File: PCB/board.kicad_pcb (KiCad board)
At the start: 2 copper layers, 81.6 x 88.8 mm, 165 parts, among them J1 Micro_SD_Card, J10 Conn_01x10, J11 Conn_01x02, J12 Conn_02x04_Odd_Even, J13 Conn_01x02, J14 Conn_01x02, J15 Conn_01x03, J16 Conn_01x02, J17 Conn_01x05, J18 Conn_01x04, J19 Conn_01x04, J2 Conn_ARM_JTAG_SWD_10, J20 Conn_01x02, J21 Conn_01x03, J22 Conn_02x04_Odd_Even, J23 Conn_01x04, J24 Conn_01x04, J25 Conn_01x02, J26 Conn_01x03, J27 Conn_02x04_Odd_Even, J28 Conn_01x04, J29 Conn_01x04, J3 USB_C_Receptacle_USB2.0_14P, J30 Conn_01x02, J31 Conn_01x03, J32 Conn_01x02, J33 Conn_01x02, J34 Conn_01x02, J35 Conn_01x02, J36 Conn_01x02, J37 Conn_01x02, J4 Conn_01x04, J5 Conn_01x04, J6 Conn_01x02, J7 Conn_01x03, J8 Conn_02x04_Odd_Even, J9 Conn_01x10, Q1 IRLML6402, Q2 NMOS, Q3 NMOS, Q4 NMOS, Q5 Q_NMOS_GDS, Q7 Q_NMOS_GDS, SW1 SW_Push, SW2 SW_Push, U1 STM32H743VITx, U2 AP7361C, U4 TMC Stepstick, U5 TMC Stepstick, U6 TMC Stepstick, U7 TMC Stepstick, U8 AP63203WU, Y2 25 MHz

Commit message: some journal stuff and starting the routing
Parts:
- moved H1 0.40 mm to (220.9, 28.1)
- moved H3 0.40 mm to (158.4, 28.1)
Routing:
- added copper zone on In2.Cu, net +3.3V
- added copper zone on In1.Cu, net GND
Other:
- copper layers 2 -> 4
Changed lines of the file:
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@@
 	(layers
 		(0 "F.Cu" signal)
+		(4 "In1.Cu" signal "GND")
+		(6 "In2.Cu" signal "POWER")
 		(2 "B.Cu" signal)
 		(9 "F.Adhes" user "F.Adhesive")
@@
 			)
 			(layer "dielectric 1"
+				(type "prepreg")
+				(thickness 0.1)
+				(material "FR4")
+				(epsilon_r 4.5)
+				(loss_tangent 0.02)
+			)
+			(layer "In1.Cu"
+				(type "copper")
+				(thickness 0.035)
+			)
+			(layer "dielectric 2"
 				(type "core")
-				(thickness 1.51)
+				(thickness 1.24)
+				(material "FR4")
+				(epsilon_r 4.5)
+				(loss_tangent 0.02)
+			)
+			(layer "In2.Cu"
+				(type "copper")
+				(thickness 0.035)
+			)
+			(layer "dielectric 3"
+				(type "prepreg")
+				(thickness 0.1)
 				(material "FR4")
 				(epsilon_r 4.5)
@@
 		(tags "Through hole pin header THT 1x04 2.00mm single row")
 		(property "Reference" "J19"
-			(at 0 -2.11 90)
+			(at -0.02875 -2.402651 180)
 			(layer "F.SilkS")
 			(effects
@@
 		(tags "Through hole pin header THT 2x04 2.00mm double row")
 		(property "Reference" "J12"
-			(at 1 -2.11 90)
+			(at 4.26625 -0.102651 180)
 			(layer "F.SilkS")
 			(effects
@@
 		(tags "connector JST XH vertical boss")
 		(property "Reference" "J4"
-			(at 3.75 -3.55 0)
+			(at 3.725 4.675 0)
 			(layer "F.SilkS")
 			(effects
@@
 		(tags "capacitor")
 		(property "Reference" "C27"
-			(at 0 -1.43 0)
+			(at 0.075 -1.50375 0)
 			(layer "F.SilkS")
 			(effects
@@
 		(tags "capacitor")
 		(property "Reference" "C7"
-			(at 0.85 -1.6 0)
+			(at -0.125 1.55 0)
 			(layer "F.SilkS")
 			(effects
@@
 	(footprint "MountingHole:MountingHole_3.2mm_M3_Pad_TopBottom"
 		(layer "F.Cu")
-		(at 158.45 28.45)
+		(at 158.45 28.05)
 		(descr "Mounting Hole 3.2mm, M3, generated by kicad-footprint-generator mountinghole.py")
 		(tags "mountinghole M3")
 		(property "Reference" "H3"
-			(at 0 -4.15 0)
+			(at -3.6 -3.075 0)
 			(layer "F.SilkS")
 			(effects
@@
 		(tags "Through hole pin header THT 1x02 2.54mm single row")
 		(property "Reference" "J11"
-			(at 0 -2.38 90)
+			(at 0.00375 5.7 0)
 			(layer "F.SilkS")
 			(effects
@@
 		(tags "resistor")
 		(property "Reference" "R25"
-			(at 0 -1.43 90)
+			(at -2.34375 -0.875 180)
 			(layer "F.SilkS")
 			(effects
@@
 		(tags "LQFP QFP")
 		(property "Reference" "U1"
-			(at 15.68 -9.43 0)
+			(at -0.025 0.05 0)
 			(layer "F.SilkS")
 			(effects
@@
 		(tags "resistor")
 		(property "Reference" "R18"
-			(at 0 -1.43 90)
+			(at -2.38375 -0.55 180)
 			(layer "F.SilkS")
 			(effects
@@
 		(tags "connector JST XH vertical boss")
 		(property "Reference" "J28"
-			(at 3.75 -3.55 0)
+			(at 3.325 4.7 0)
 			(layer "F.SilkS")
 			(effects
@@
 	(footprint "MountingHole:MountingHole_3.2mm_M3_Pad_TopBottom"
 		(layer "F.Cu")
-		(at 220.9 108.65)
+		(at 220.9 108.7)
 		(descr "Mounting Hole 3.2mm, M3, generated by kicad-footprint-generator mountinghole.py")
 		(tags "mountinghole M3")
@@
 		(tags "Through hole pin header THT 1x02 2.54mm single row")
 		(property "Reference" "J30"
-			(at 0 -2.38 90)
+			(at -0.05625 5.65 180)
 			(layer "F.SilkS")
 			(effects
@@
 		(tags "resistor")
 		(property "Reference" "R21"
-			(at 0 -1.43 90)
+			(at -2.14375 -0.727651 180)
 			(layer "F.SilkS")
 			(effects
@@
 		(tags "Through hole pin header THT 2x04 2.00mm double row")
 		(property "Reference" "J27"
-			(at 1 -2.11 90)
+			(at 4.40875 -0.2 180)
 			(layer "F.SilkS")
 			(effects
@@
 		(tags "Through hole pin header THT 2x04 2.00mm double row")
 		(property "Reference" "J22"
-			(at 1 -2.11 90)
+			(at 4.35625 -0.225 180)
 			(layer "F.SilkS")
 			(effects
@@
 		(tags "Through hole pin header THT 1x02 2.54mm single row")
 		(property "Reference" "J20"
-			(at 0 -2.38 90)
+			(at -0.09375 5.547349 180)
 			(layer "F.SilkS")
 			(effects
@@
 		(tags "resistor")
 		(property "Reference" "R29"
-			(at 0 -1.43 0)
+			(at 0.04 1.445 0)
 			(layer "F.SilkS")
 			(effects
@@
 		(tags "connector JST XH vertical")
 		(property "Reference" "J7"
-			(at 2.5 -3.55 0)
+			(at 8.975 2.78125 0)
 			(layer "F.SilkS")
 			(effects
@@
 		(tags "capacitor")
 		(property "Reference" "C8"
-			(at 0 -1.43 45)
+			(at 0 -1.43 225)
 			(layer "F.SilkS")
 			(effects
@@
 		(tags "capacitor")
 		(property "Reference" "C29"
-			(at 0 -1.43 0)
+			(at -0.05 -1.49625 0)
 			(layer "F.SilkS")
 			(effects
@@
 		(tags "Through hole pin header THT 1x04 2.00mm single row")
 		(property "Reference" "J29"
-			(at 0 -2.11 90)
+			(at 0.1025 -2.925 180)
 			(layer "F.SilkS")
 			(effects
@@
 		(tags "resistor")
 		(property "Reference" "R31"
-			(at 0 -1.43 0)
+			(at 3.005 0.0225 0)
 			(layer "F.SilkS")
 			(effects
@@
 		(tags "Through hole pin header THT 1x04 2.00mm single row")
 		(property "Reference" "J24"
-			(at 0 -2.11 90)
+			(at 0 -2.9 180)
 			(layer "F.SilkS")
 			(effects
@@
 		(tags "Through hole pin header THT 2x04 2.00mm double row")
 		(property "Reference" "J8"
-			(at 1 -2.11 90)
+			(at 4.22875 -0.625 0)
 			(layer "F.SilkS")
 			(effects
@@
 		(tags "capacitor")
 		(property "Reference" "C30"
-			(at 0 -1.43 0)
+			(at -3.075 -0.21875 0)
 			(layer "F.SilkS")
 			(effects
@@
 		(tags "capacitor")
 		(property "Reference" "C38"
-			(at 0 -1.43 0)
+			(at 2.75 0.03125 0)
 			(layer "F.SilkS")
 			(effects
@@
 		(tags "Through hole pin header THT 1x04 2.00mm single row")
 		(property "Reference" "J5"
-			(at 0 -2.11 90)
+			(at -0.19375 -2.425 0)
 			(layer "F.SilkS")
 			(effects
@@
 		(tags "capacitor")
 		(property "Reference" "C1"
-			(at 0 -1.68 90)
+			(at 0.05 -2 180)
 			(layer "F.SilkS")
 			(effects
@@
 		(tags "connector JST XH vertical boss")
 		(property "Reference" "J18"
-			(at 3.75 -3.55 0)
+			(at 3.675 4.625 0)
 			(layer "F.SilkS")
 			(effects
@@
 		(tags "capacitor")
 		(property "Reference" "C34"
-			(at 0 -1.43 0)
+			(at -2.922349 -0.16875 0)
 			(layer "F.SilkS")
 			(effects
@@
 	(footprint "MountingHole:MountingHole_3.2mm_M3_Pad_TopBottom"
 		(layer "F.Cu")
-		(at 220.9 28.45)
+		(at 220.9 28.05)
 		(descr "Mounting Hole 3.2mm, M3, generated by kicad-footprint-generator mountinghole.py")
 		(tags "mountinghole M3")
@@
 		(descr "SMD3225/4, Crystal, 3.2x2.5mm package, SMD, generated with kicad-footprint-generator make_crystal.py, http://www.txccrystal.com/images/pdf/7m-accuracy.pdf")
 		(property "Reference" "Y2"
-			(at 0 -2.45 90)
+			(at -1.45 -2.7 180)
 			(layer "F.SilkS")
 			(effects
@@
 		(tags "Through hole pin header THT 1x02 2.54mm single row")
 		(property "Reference" "J25"
-			(at 0 -2.38 90)
+			(at -0.01875 5.725 180)
 			(layer "F.SilkS")
 			(effects
@@
 		(tags "connector JST XH vertical boss")
 		(property "Reference" "J23"
-			(at 3.75 -3.55 0)
+			(at 3.3 4.8 0)
 			(layer "F.SilkS")
 			(effects
@@
 		(tags "Through hole vertical IDC box header THT 2x05 2.54mm double row")
 		(property "Reference" "J10"
-			(at 1.27 -6.1 0)
+			(at 7.425 -4.125 0)
 			(layer "F.SilkS")
 			(effects
@@
 		(tags "capacitor")
 		(property "Reference" "C11"
-			(at 0 -1.43 0)
+			(at -3.025 0.225 0)
 			(layer "F.SilkS")
 			(effects
@@
 		(layer "Edge.Cuts")
 	)
+	(zone
+		(net 2)
+		(net_name "GND")
+		(layer "In1.Cu")
+		(hatch edge 0.5)
+		(connect_pads
+			(clearance 0.5)
+		)
+		(min_thickness 0.25)
+		(filled_areas_thickness no)
+		(fill yes
+			(thermal_gap 0.5)
+			(thermal_bridge_width 0.5)
+		)
+		(polygon
+			(pts
+				(xy 235.275 23.95) (xy 153.625 23.95) (xy 153.625 112.8) (xy 235.275 112.8)
+			)
+		)
+	)
+	(zone
+		(net 4)
+		(net_name "+3.3V")
+		(layer "In2.Cu")
+		(hatch edge 0.5)
+		(priority 1)
+		(connect_pads
+			(clearance 0.5)
+		)
+		(min_thickness 0.25)
+		(filled_areas_thickness no)
+		(fill yes
+			(thermal_gap 0.5)
+			(thermal_bridge_width 0.5)
+		)
+		(polygon
+			(pts
+				(xy 235.275 23.95) (xy 153.625 23.95) (xy 153.625 112.8) (xy 235.275 112.8)
+			)
+		)
+	)
 	(group ""

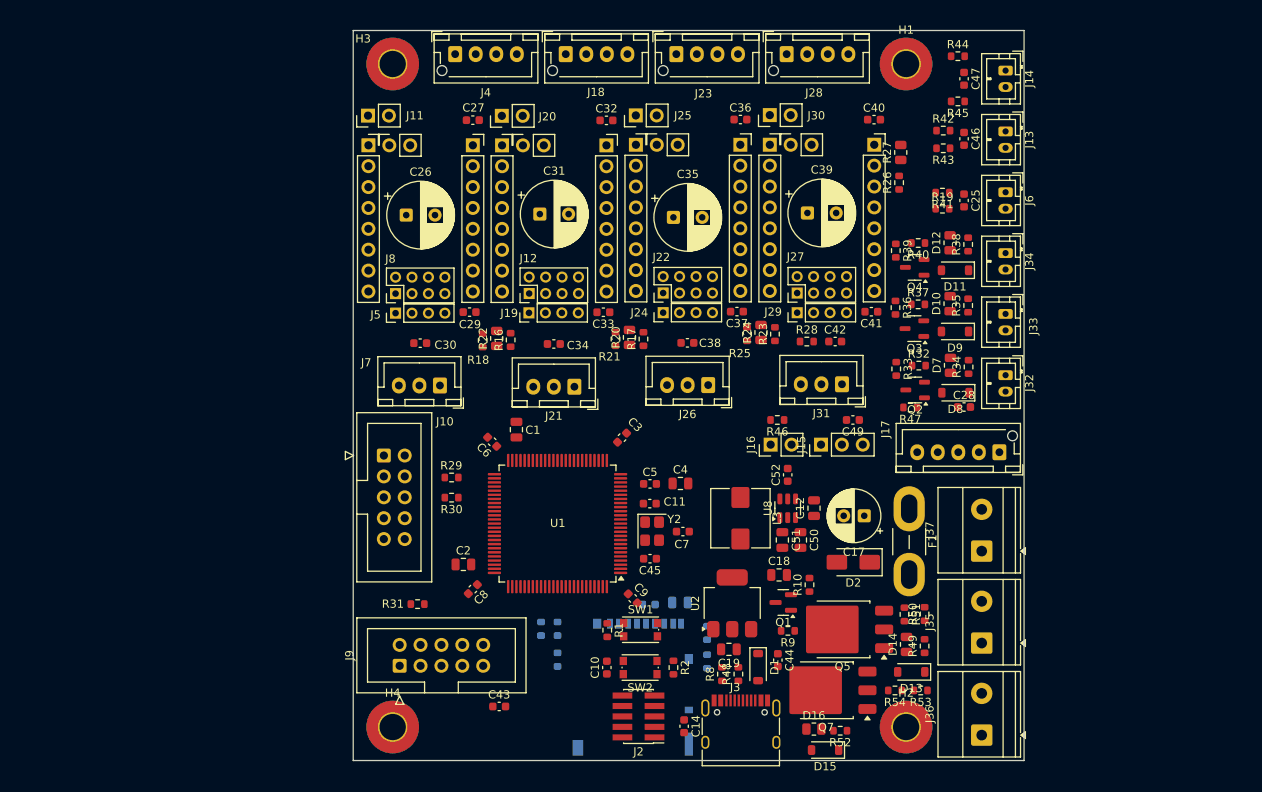
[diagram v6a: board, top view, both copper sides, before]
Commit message: started to via all the grounds down
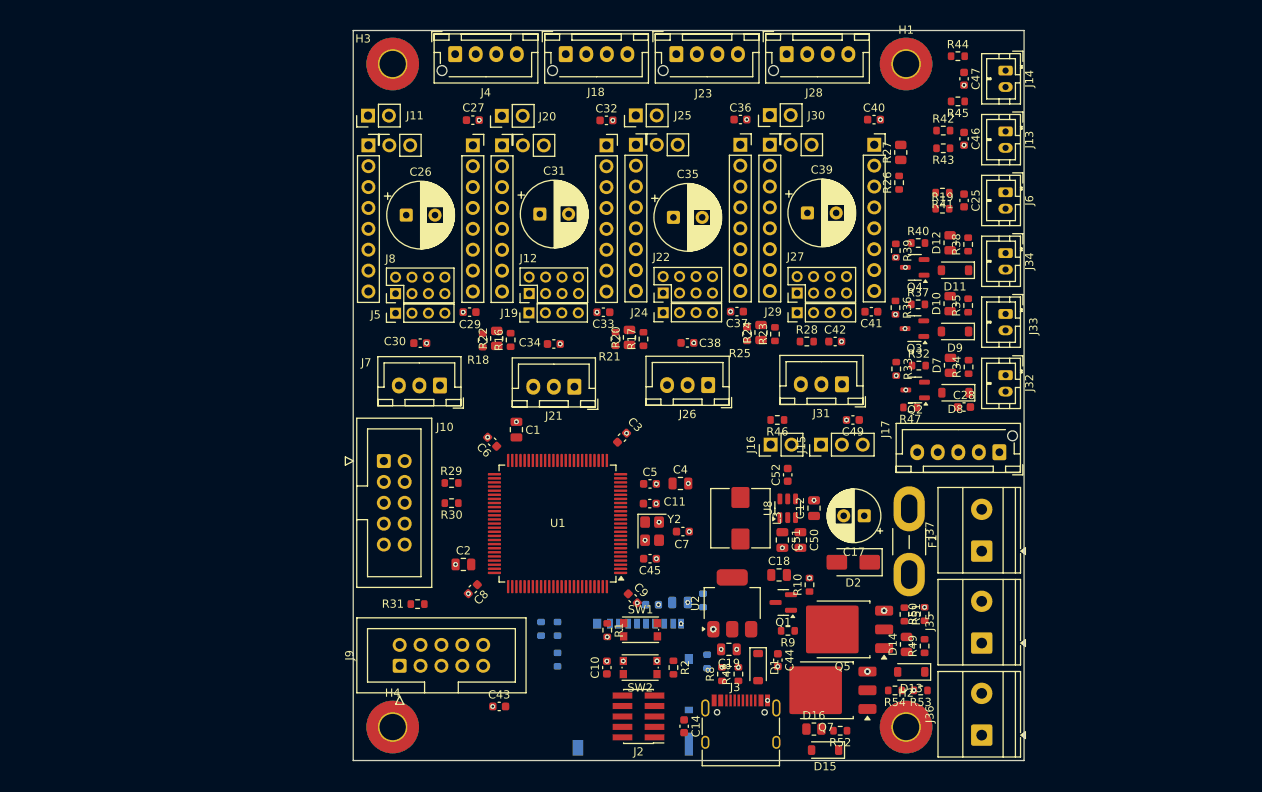
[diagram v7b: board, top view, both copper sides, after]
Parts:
- moved R7 3.98 mm to (196.2, 93.3)
- moved J10 0.67 mm to (157.4, 76.3)
- moved R29 0.67 mm to (165.6, 79.0)
- moved R30 0.67 mm to (165.6, 81.5)
- moved C15 0.40 mm to (190.0, 93.8)
- turned C30 to 0 degrees
- turned C34 to 0 degrees
- turned R40 to 0 degrees
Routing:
- net GND: vias 0 -> 55
- net +5V: vias 0 -> 1
- added copper zone on In2.Cu, net +5V

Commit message: lots of powers and gnd's via'd too, I don't really know how to say it lol
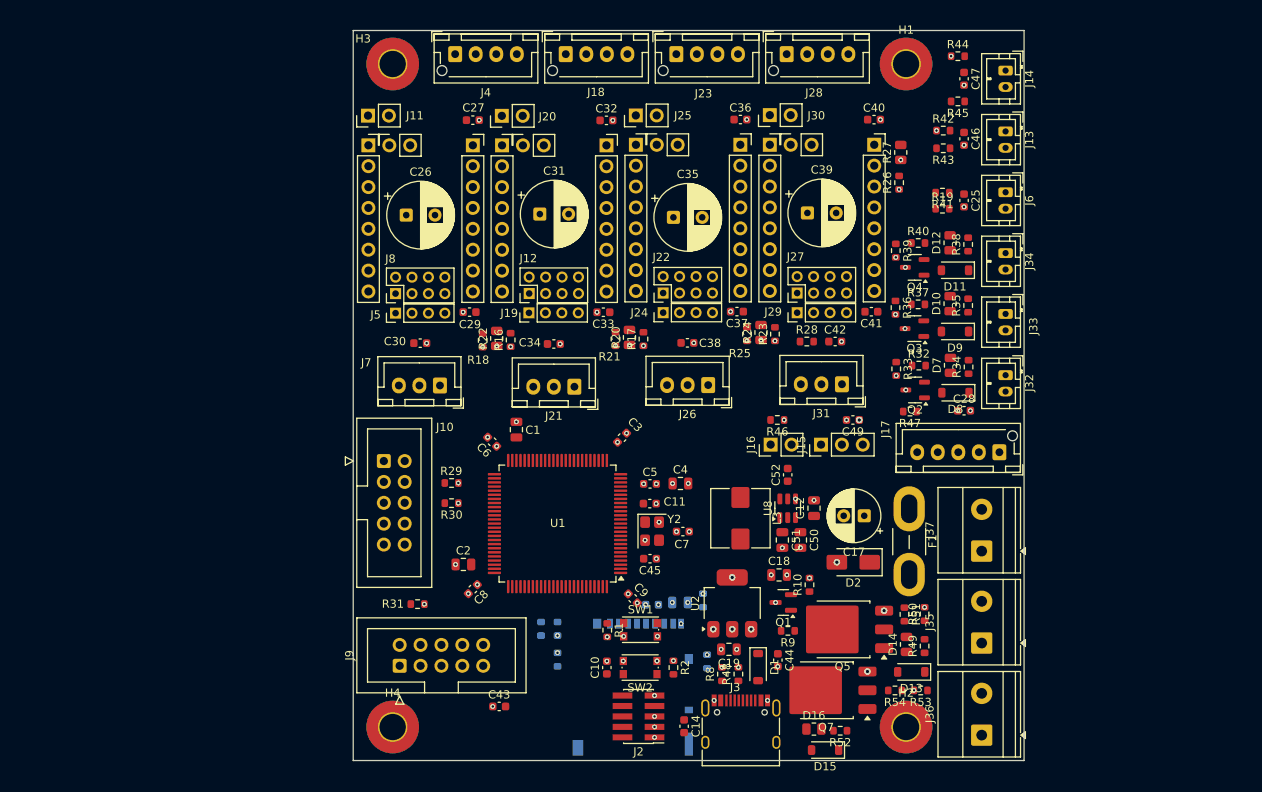
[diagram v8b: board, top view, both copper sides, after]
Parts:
- moved R47 0.50 mm to (221.4, 70.3)
- moved C28 0.45 mm to (227.9, 70.2)
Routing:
- net GND: vias 55 -> 64
- net +5V: vias 1 -> 5
- net +3.3V: vias 0 -> 37
